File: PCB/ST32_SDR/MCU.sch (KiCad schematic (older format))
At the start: 13 parts, among them U2 FM24CL16B, U3 STM32F401RCTx, Y1 20Mhz

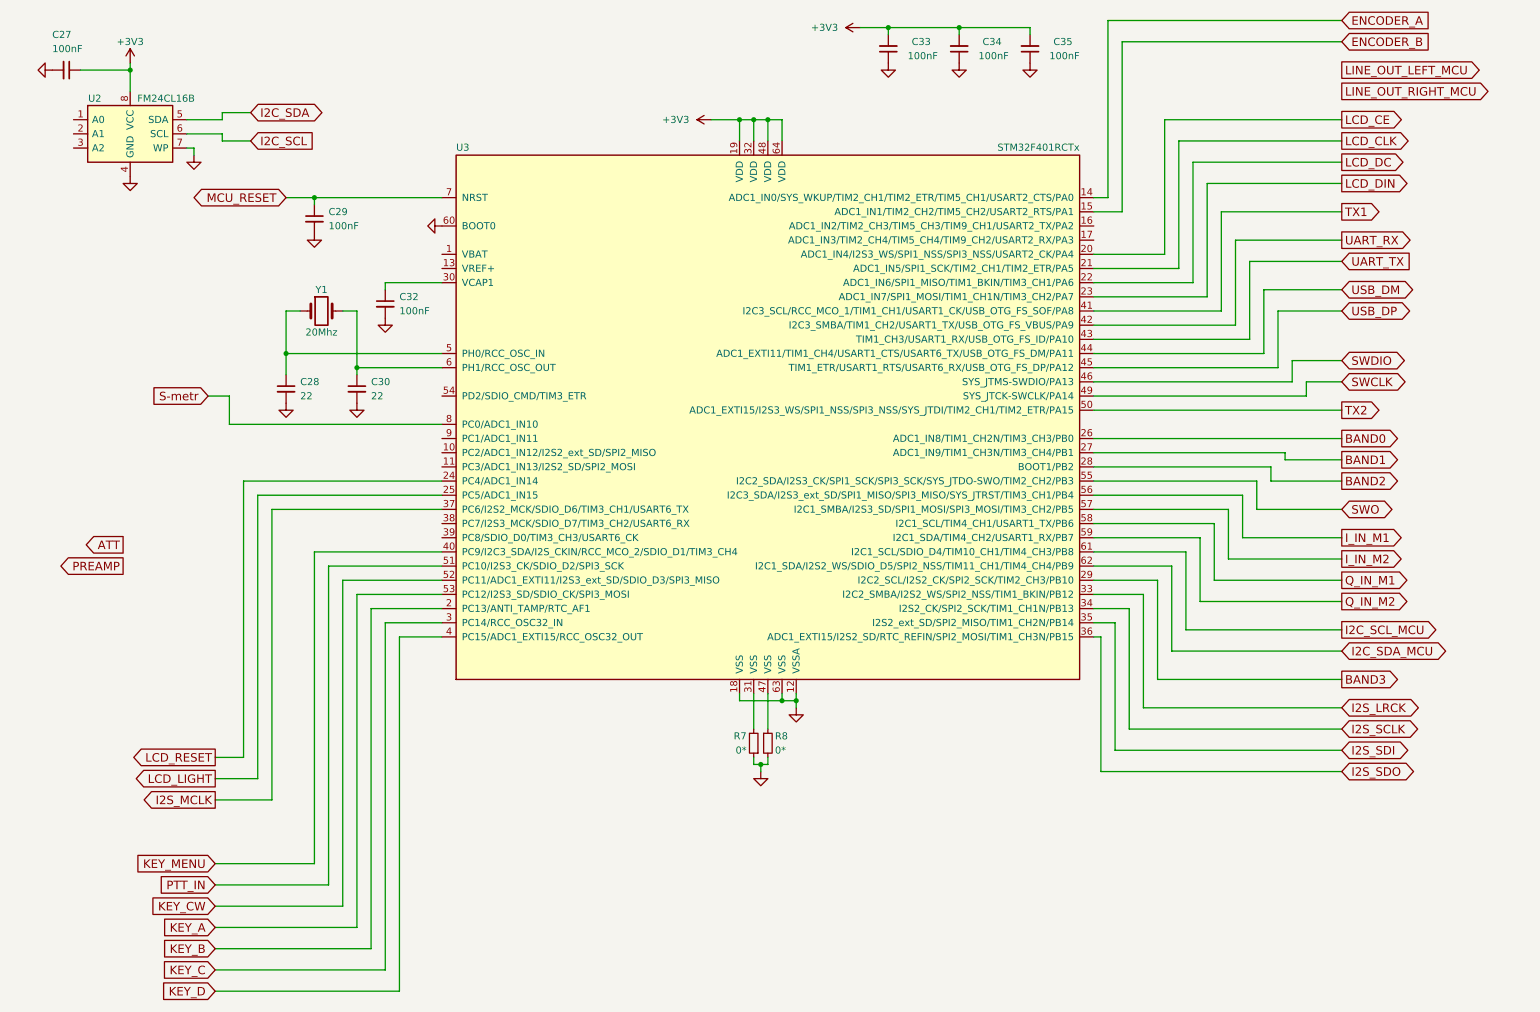
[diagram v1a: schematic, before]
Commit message: LCD at SPI3
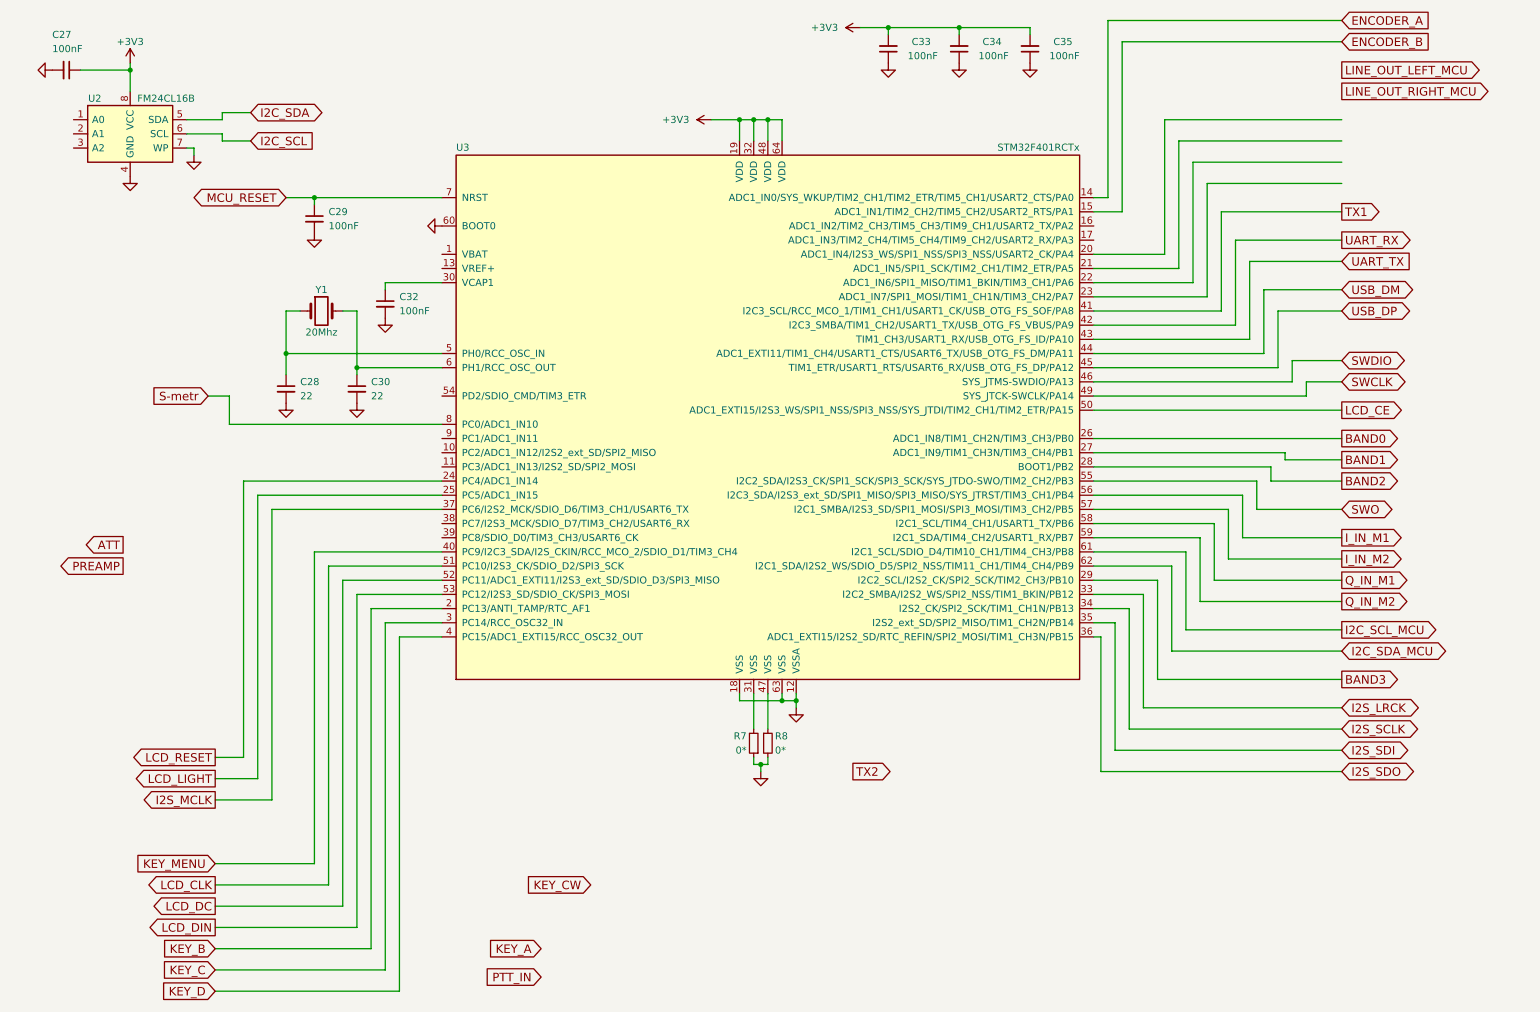
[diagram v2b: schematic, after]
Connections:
- net KEY_A: no longer U3.53 (PC12/I2S3_SD/SDIO_CK/SPI3_MOSI)
- net KEY_CW: no longer U3.52 (PC11/ADC1_EXTI11/I2S3_ext_SD/SDIO_D3/SPI3_MISO)
- net LCD_CE: now also U3.50 (ADC1_EXTI15/I2S3_WS/SPI1_NSS/SPI3_NSS/SYS_JTDI/TIM2_CH1/TIM2_ETR/PA15); no longer U3.20 (ADC1_IN4/I2S3_WS/SPI1_NSS/SPI3_NSS/USART2_CK/PA4)
- net LCD_CLK: now also U3.51 (PC10/I2S3_CK/SDIO_D2/SPI3_SCK); no longer U3.21 (ADC1_IN5/SPI1_SCK/TIM2_CH1/TIM2_ETR/PA5)
- net LCD_DC: now also U3.52 (PC11/ADC1_EXTI11/I2S3_ext_SD/SDIO_D3/SPI3_MISO); no longer U3.22 (ADC1_IN6/SPI1_MISO/TIM1_BKIN/TIM3_CH1/PA6)
- net LCD_DIN: now also U3.53 (PC12/I2S3_SD/SDIO_CK/SPI3_MOSI); no longer U3.23 (ADC1_IN7/SPI1_MOSI/TIM1_CH1N/TIM3_CH2/PA7)
- net PTT_IN: no longer U3.51 (PC10/I2S3_CK/SDIO_D2/SPI3_SCK)
- net TX2: no longer U3.50 (ADC1_EXTI15/I2S3_WS/SPI1_NSS/SPI3_NSS/SYS_JTDI/TIM2_CH1/TIM2_ETR/PA15)
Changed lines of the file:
@@
 LIBS:4ms-ic
 LIBS:Display
-LIBS:Connector
-LIBS:Relay
+LIBS:switches
+LIBS:cmos4000
 LIBS:LCSDR-cache
 EELAYER 25 0
@@
 	3250 2450 3250 2500
 $Comp
-L GND #PWR45
+L GND #PWR035
 U 1 1 5DD64FC0
 P 5900 5900
-F 0 "#PWR45" H 5900 5650 50  0001 C CNN
+F 0 "#PWR035" H 5900 5650 50  0001 C CNN
 F 1 "GND" H 5900 5750 50  0001 C CNN
 F 2 "" H 5900 5900 50  0001 C CNN
@@
 	5950 5350 5950 5600
 $Comp
-L GND #PWR46
+L GND #PWR036
 U 1 1 5DD650F1
 P 6150 5450
-F 0 "#PWR46" H 6150 5200 50  0001 C CNN
+F 0 "#PWR036" H 6150 5200 50  0001 C CNN
 F 1 "GND" H 6150 5300 50  0001 C CNN
 F 2 "" H 6150 5450 50  0001 C CNN
@@
 Connection ~ 6150 5400
 $Comp
-L GND #PWR42
+L GND #PWR037
 U 1 1 5DD65332
 P 3250 2700
-F 0 "#PWR42" H 3250 2450 50  0001 C CNN
+F 0 "#PWR037" H 3250 2450 50  0001 C CNN
 F 1 "GND" H 3250 2550 50  0001 C CNN
 F 2 "" H 3250 2700 50  0001 C CNN
@@
 	2550 2950 3650 2950
 $Comp
-L GND #PWR41
+L GND #PWR038
 U 1 1 5DD65598
 P 3050 3300
-F 0 "#PWR41" H 3050 3050 50  0001 C CNN
+F 0 "#PWR038" H 3050 3050 50  0001 C CNN
 F 1 "GND" H 3050 3150 50  0001 C CNN
 F 2 "" H 3050 3300 50  0001 C CNN
@@
 $EndComp
 $Comp
-L GND #PWR39
+L GND #PWR039
 U 1 1 5DD655DB
 P 2550 3300
-F 0 "#PWR39" H 2550 3050 50  0001 C CNN
+F 0 "#PWR039" H 2550 3050 50  0001 C CNN
 F 1 "GND" H 2550 3150 50  0001 C CNN
 F 2 "" H 2550 3300 50  0001 C CNN
@@
 	2750 1850 2750 1900
 $Comp
-L GND #PWR40
+L GND #PWR040
 U 1 1 5DD65924
 P 2750 2100
-F 0 "#PWR40" H 2750 1850 50  0001 C CNN
+F 0 "#PWR040" H 2750 1850 50  0001 C CNN
 F 1 "GND" H 2750 1950 50  0001 C CNN
 F 2 "" H 2750 2100 50  0001 C CNN
@@
 $EndComp
 $Comp
-L GND #PWR37
+L GND #PWR041
 U 1 1 5DD66640
 P 1450 1700
-F 0 "#PWR37" H 1450 1450 50  0001 C CNN
+F 0 "#PWR041" H 1450 1450 50  0001 C CNN
 F 1 "GND" H 1450 1550 50  0001 C CNN
 F 2 "" H 1450 1700 50  0001 C CNN
@@
 $EndComp
 $Comp
-L GND #PWR38
+L GND #PWR042
 U 1 1 5DD667F8
 P 1900 1550
-F 0 "#PWR38" H 1900 1300 50  0001 C CNN
+F 0 "#PWR042" H 1900 1300 50  0001 C CNN
 F 1 "GND" H 1900 1400 50  0001 C CNN
 F 2 "" H 1900 1550 50  0001 C CNN
@@
 	2100 1450 2300 1450
 $Comp
-L +3V3 #PWR36
+L +3V3 #PWR043
 U 1 1 5DD9FC90
 P 1450 900
-F 0 "#PWR36" H 1450 750 50  0001 C CNN
+F 0 "#PWR043" H 1450 750 50  0001 C CNN
 F 1 "+3V3" H 1450 1050 50  0000 C CNN
 F 2 "" H 1450 900 50  0001 C CNN
@@
 Connection ~ 1450 950
 $Comp
-L GND #PWR35
+L GND #PWR044
 U 1 1 5DDA00B4
 P 900 950
-F 0 "#PWR35" H 900 700 50  0001 C CNN
+F 0 "#PWR044" H 900 700 50  0001 C CNN
 F 1 "GND" H 900 800 50  0001 C CNN
 F 2 "" H 900 950 50  0001 C CNN
@@
 $EndComp
 $Comp
-L +3V3 #PWR44
+L +3V3 #PWR045
 U 1 1 5DDA012B
 P 5550 1300
-F 0 "#PWR44" H 5550 1150 50  0001 C CNN
+F 0 "#PWR045" H 5550 1150 50  0001 C CNN
 F 1 "+3V3" V 5550 1550 50  0000 C CNN
 F 2 "" H 5550 1300 50  0001 C CNN
@@
 Connection ~ 5750 1300
 $Comp
-L +3V3 #PWR47
+L +3V3 #PWR046
 U 1 1 5DDA0C93
 P 6600 650
-F 0 "#PWR47" H 6600 500 50  0001 C CNN
+F 0 "#PWR046" H 6600 500 50  0001 C CNN
 F 1 "+3V3" V 6600 900 50  0000 C CNN
 F 2 "" H 6600 650 50  0001 C CNN
@@
 Connection ~ 6800 650
 $Comp
-L GND #PWR48
+L GND #PWR047
 U 1 1 5DDA0E68
 P 6800 900
-F 0 "#PWR48" H 6800 650 50  0001 C CNN
+F 0 "#PWR047" H 6800 650 50  0001 C CNN
 F 1 "GND" H 6800 750 50  0001 C CNN
 F 2 "" H 6800 900 50  0001 C CNN
@@
 $EndComp
 $Comp
-L GND #PWR49
+L GND #PWR048
 U 1 1 5DDA0EDC
 P 7300 900
-F 0 "#PWR49" H 7300 650 50  0001 C CNN
+F 0 "#PWR048" H 7300 650 50  0001 C CNN
 F 1 "GND" H 7300 750 50  0001 C CNN
 F 2 "" H 7300 900 50  0001 C CNN
@@
 $EndComp
 $Comp
-L GND #PWR50
+L GND #PWR049
 U 1 1 5DDA0F4B
 P 7800 900
-F 0 "#PWR50" H 7800 650 50  0001 C CNN
+F 0 "#PWR049" H 7800 650 50  0001 C CNN
 F 1 "GND" H 7800 750 50  0001 C CNN
 F 2 "" H 7800 900 50  0001 C CNN
@@
 Wire Wire Line
 	9550 2650 10000 2650
-Text GLabel 10000 1600 2    60   Output ~ 0
+Text GLabel 2050 6850 0    60   Output ~ 0
 LCD_DC
 Text GLabel 10000 2300 2    60   Input ~ 0
 UART_TX
-Text GLabel 10000 1300 2    60   Output ~ 0
+Text GLabel 10000 3350 2    60   Output ~ 0
 LCD_CE
-Text GLabel 10000 1450 2    60   Output ~ 0
+Text GLabel 2050 6700 0    60   Output ~ 0
 LCD_CLK
-Text GLabel 10000 1750 2    60   Output ~ 0
+Text GLabel 2050 7000 0    60   Output ~ 0
 LCD_DIN
 Text GLabel 10000 750  2    60   Input ~ 0
@@
 Wire Wire Line
 	3350 7450 2050 7450
-Text GLabel 2050 7000 0    60   Input ~ 0
+Text GLabel 4350 7150 0    60   Input ~ 0
 KEY_A
 Text GLabel 2050 7150 0    60   Input ~ 0
@@
 Text GLabel 2050 7450 0    60   Input ~ 0
 KEY_D
-Text GLabel 2050 6850 0    60   Input ~ 0
-KEY_CW
-Text GLabel 2050 6700 0    60   Input ~ 0
+Text GLabel 4350 7350 0    60   Input ~ 0
 PTT_IN
 Wire Wire Line
@@
 Wire Wire Line
 	8250 1850 8350 1850
-Text GLabel 10000 3350 2    60   Output ~ 0
+Text GLabel 6550 5900 2    60   Output ~ 0
 TX2
 Wire Wire Line
@@
 	9650 3000 10000 3000
 $Comp
-L GND #PWR43
+L GND #PWR050
 U 1 1 5DDFAF2B
 P 3650 2050
-F 0 "#PWR43" H 3650 1800 50  0001 C CNN
+F 0 "#PWR050" H 3650 1800 50  0001 C CNN
 F 1 "GND" H 3650 1900 50  0001 C CNN
 F 2 "" H 3650 2050 50  0001 C CNN
@@
 Text GLabel 10000 1100 2    60   Output ~ 0
 LINE_OUT_RIGHT_MCU
+Text GLabel 4700 6700 0    60   Input ~ 0
+KEY_CW
 $EndSCHEMATC

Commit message: PCB Windows 1
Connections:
- net labels removed: I_IN_M1
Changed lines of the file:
@@
 LIBS:4ms-ic
 LIBS:Display
-LIBS:Connector
-LIBS:Relay
+LIBS:switches
+LIBS:cmos4000
 LIBS:LCSDR-cache
 EELAYER 25 0
@@
 Text GLabel 10000 5450 2    60   BiDi ~ 0
 I2S_LRCK
-Text GLabel 10000 4900 2    60   Output ~ 0
+Text GLabel 10000 1950 2    60   Output ~ 0
 I2C_SCL_MCU
-Text GLabel 10000 5050 2    60   BiDi ~ 0
+Text GLabel 2050 6550 0    60   BiDi ~ 0
 I2C_SDA_MCU
 Wire Wire Line
@@
 	1    0    0    -1
 $EndComp
-Text GLabel 10000 2150 2    60   Output ~ 0
+Text GLabel 10700 2100 2    60   Output ~ 0
 UART_RX
 Wire Wire Line
@@
 Text GLabel 2050 6850 0    60   Output ~ 0
 LCD_DC
-Text GLabel 10000 2300 2    60   Input ~ 0
+Text GLabel 10750 3000 2    60   Input ~ 0
 UART_TX
 Text GLabel 10000 3350 2    60   Output ~ 0
@@
 Text GLabel 2050 7000 0    60   Output ~ 0
 LCD_DIN
-Text GLabel 10000 750  2    60   Input ~ 0
+Text GLabel 10000 1750 2    60   Input ~ 0
 ENCODER_B
-Text GLabel 10000 600  2    60   Input ~ 0
+Text GLabel 10000 1600 2    60   Input ~ 0
 ENCODER_A
 Wire Wire Line
@@
 Wire Wire Line
 	2850 4450 3650 4450
-Wire Wire Line
-	2150 3250 2000 3250
-Text GLabel 2000 3250 0    60   Input ~ 0
+Text GLabel 1950 3800 0    60   Input ~ 0
 S-metr
-Text GLabel 2050 6550 0    60   Input ~ 0
+Text GLabel 1350 5800 0    60   Input ~ 0
 KEY_MENU
 Wire Wire Line
@@
 	2550 2650 2650 2650
 Connection ~ 2550 2950
-Wire Wire Line
-	2150 3450 2150 3250
 Text GLabel 2550 1850 0    60   BiDi ~ 0
 MCU_RESET
@@
 Text GLabel 10000 4400 2    60   Output ~ 0
 I_IN_M2
-Text GLabel 10000 4250 2    60   Output ~ 0
-I_IN_M1
 Wire Wire Line
 	8250 4250 9000 4250
@@
 Text GLabel 10000 3550 2    60   Output ~ 0
 BAND0
-Wire Wire Line
-	2150 3450 3650 3450
 Text GLabel 10000 3700 2    60   Output ~ 0
 BAND1
@@
 Wire Wire Line
 	2450 6100 2450 4050
-Text GLabel 2050 5800 0    60   Output ~ 0
+Text GLabel 1900 3450 0    60   Output ~ 0
 LCD_RESET
-Text GLabel 2050 5950 0    60   Output ~ 0
+Text GLabel 10000 4250 2    60   Output ~ 0
 LCD_LIGHT
 Wire Wire Line
@@
 Wire Wire Line
 	8700 4550 8250 4550
-Text GLabel 10000 1950 2    60   Output ~ 0
+Text GLabel 10750 1750 2    60   Output ~ 0
 TX1
 Wire Wire Line
@@
 Text GLabel 4700 6700 0    60   Input ~ 0
 KEY_CW
+Wire Wire Line
+	1900 3450 3350 3450
+Wire Wire Line
+	3350 3450 3350 3250
+Wire Wire Line
+	3350 3250 3650 3250
 $EndSCHEMATC

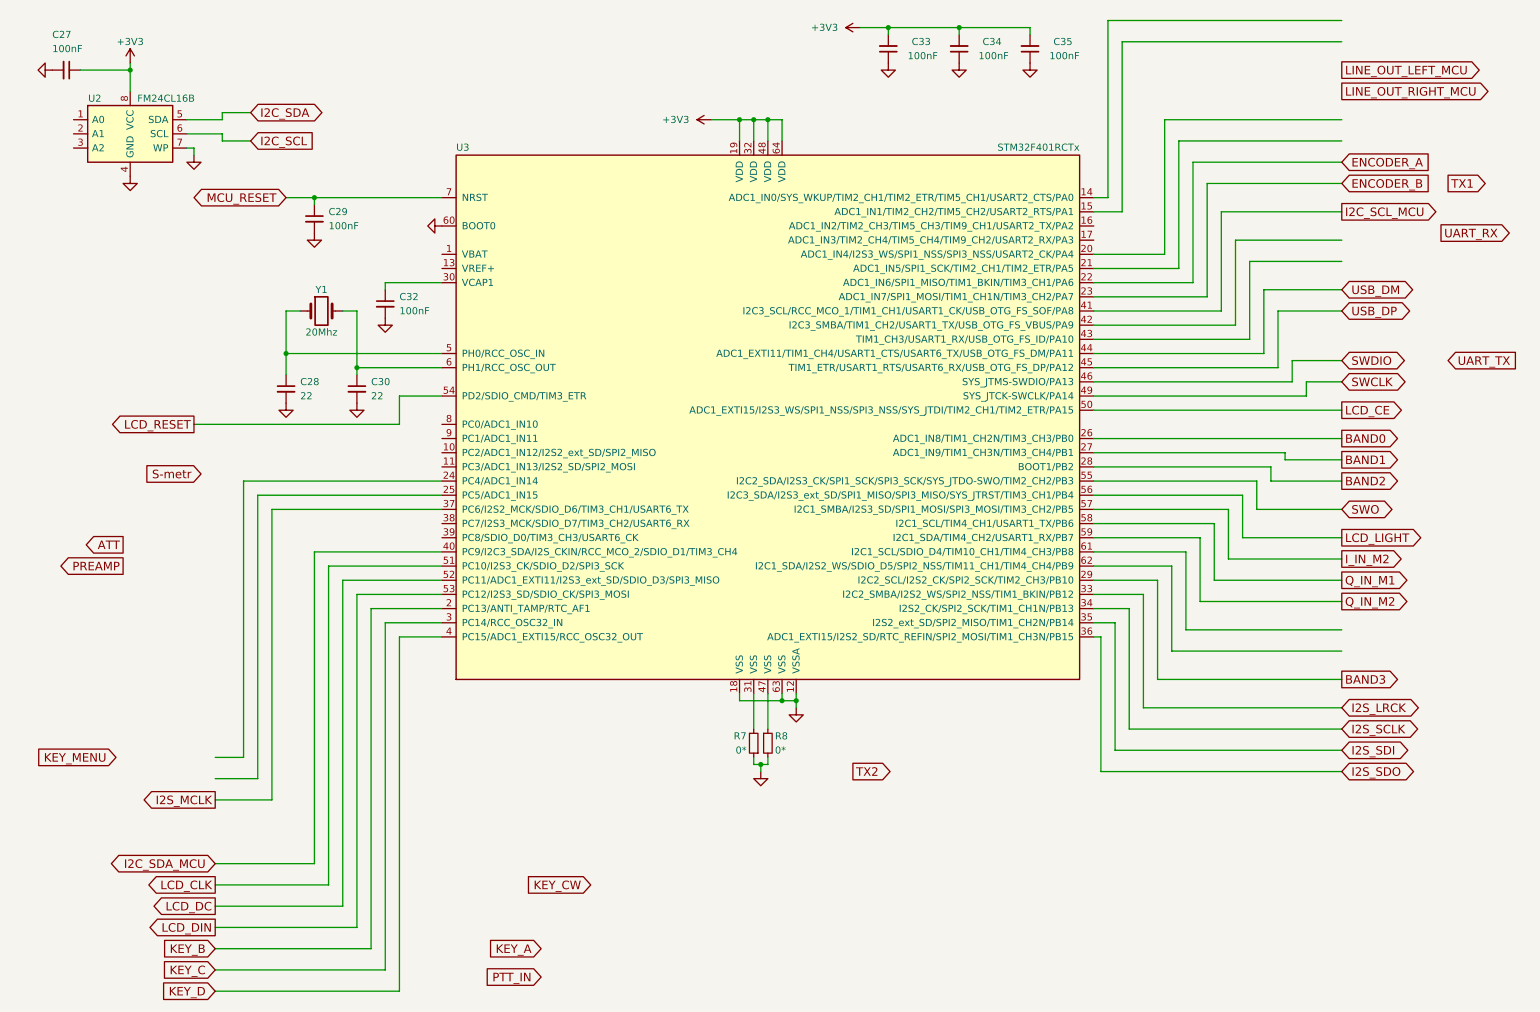
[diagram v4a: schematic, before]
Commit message: PCB Linux 2, update AUDIO_OUT
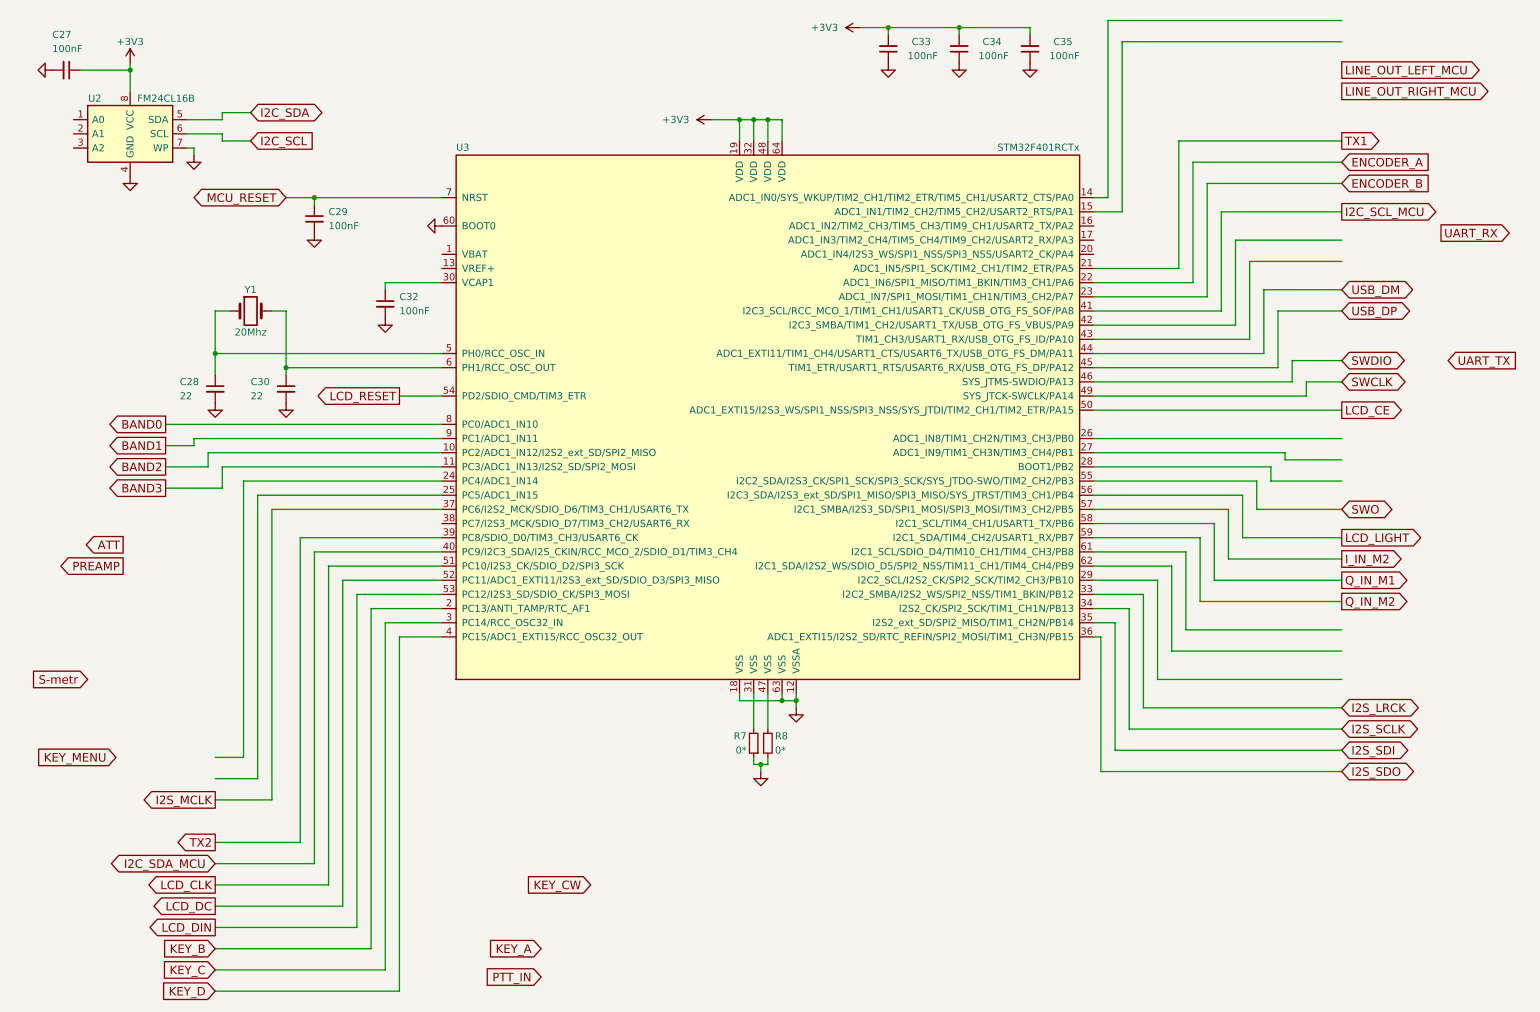
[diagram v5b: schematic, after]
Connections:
- wire segments 155 -> 163
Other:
- moved on the sheet: C28, C30, Y1
